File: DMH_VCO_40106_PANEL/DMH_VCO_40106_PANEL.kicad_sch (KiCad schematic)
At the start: 35 parts, among them J1 GND

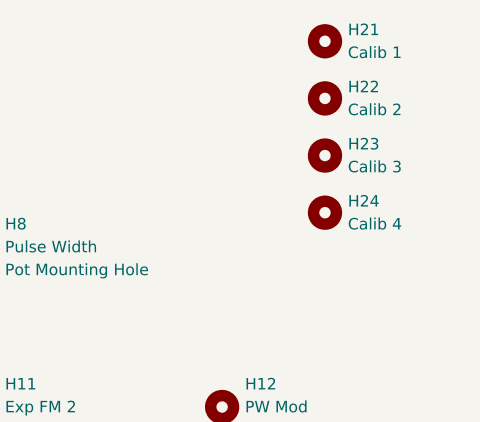
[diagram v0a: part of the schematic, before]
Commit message: Updated pot mounting hole sizes
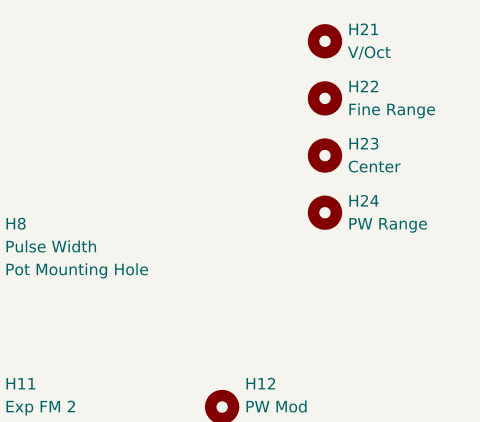
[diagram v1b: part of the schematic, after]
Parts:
- H21: value Calib 1 -> V/Oct; footprint MountingHole:MountingHole_2.2mm_M2_DIN965 -> MountingHole:MountingHole_2.5mm
- H22: value Calib 2 -> Fine Range; footprint MountingHole:MountingHole_2.2mm_M2_DIN965 -> MountingHole:MountingHole_2.5mm
- H23: value Calib 3 -> Center; footprint MountingHole:MountingHole_2.2mm_M2_DIN965 -> MountingHole:MountingHole_2.5mm
- H24: value Calib 4 -> PW Range; footprint MountingHole:MountingHole_2.2mm_M2_DIN965 -> MountingHole:MountingHole_2.5mm
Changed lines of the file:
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@@
 			)
 		)
-		(property "Value" "Calib 3"
+		(property "Value" "Center"
 			(at 180.34 31.7499 0)
 			(effects
@@
 			)
 		)
-		(property "Footprint" "MountingHole:MountingHole_2.2mm_M2_DIN965"
+		(property "Footprint" "MountingHole:MountingHole_2.5mm"
 			(at 177.8 30.48 0)
 			(effects
@@
 			)
 		)
-		(property "Value" "Calib 1"
+		(property "Value" "V/Oct"
 			(at 180.34 19.0499 0)
 			(effects
@@
 			)
 		)
-		(property "Footprint" "MountingHole:MountingHole_2.2mm_M2_DIN965"
+		(property "Footprint" "MountingHole:MountingHole_2.5mm"
 			(at 177.8 17.78 0)
 			(effects
@@
 			)
 		)
-		(property "Value" "Calib 4"
+		(property "Value" "PW Range"
 			(at 180.34 38.0999 0)
 			(effects
@@
 			)
 		)
-		(property "Footprint" "MountingHole:MountingHole_2.2mm_M2_DIN965"
+		(property "Footprint" "MountingHole:MountingHole_2.5mm"
 			(at 177.8 36.83 0)
 			(effects
@@
 			)
 		)
-		(property "Value" "Calib 2"
+		(property "Value" "Fine Range"
 			(at 180.34 25.3999 0)
 			(effects
@@
 			)
 		)
-		(property "Footprint" "MountingHole:MountingHole_2.2mm_M2_DIN965"
+		(property "Footprint" "MountingHole:MountingHole_2.5mm"
 			(at 177.8 24.13 0)
 			(effects

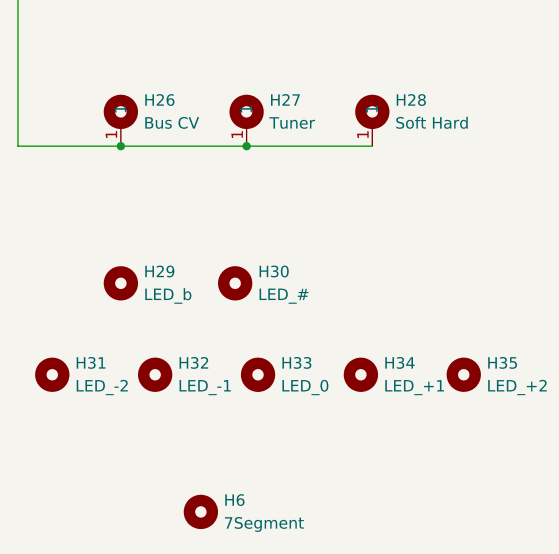
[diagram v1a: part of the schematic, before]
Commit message: Removed the flat sign LED
and rerouted segments A and B to PORTD 6 and 7 respective,
and rerouted the DP segment to PORTA0
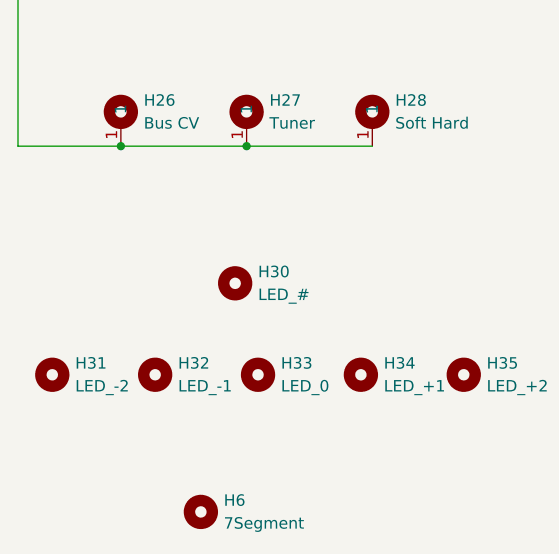
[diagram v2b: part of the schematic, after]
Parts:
- removed H29: LED_b, SynthStuff:MountingHole_LED_3mm, symbol Mechanical:MountingHole
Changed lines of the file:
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@@
-	)
-	(symbol
-		(lib_id "Mechanical:MountingHole")
-		(at 26.67 95.25 0)
-		(unit 1)
-		(exclude_from_sim yes)
-		(in_bom no)
-		(on_board yes)
-		(dnp no)
-		(fields_autoplaced yes)
-		(property "Reference" "H29"
-			(at 29.21 93.9799 0)
-			(effects
-				(font
-					(size 1.27 1.27)
-				)
-				(justify left)
-			)
-		)
-		(property "Value" "LED_b"
-			(at 29.21 96.5199 0)
-			(effects
-				(font
-					(size 1.27 1.27)
-				)
-				(justify left)
-			)
-		)
-		(property "Footprint" "SynthStuff:MountingHole_LED_3mm"
-			(at 26.67 95.25 0)
-			(effects
-				(font
-					(size 1.27 1.27)
-				)
-				(hide yes)
-			)
-		)
-		(property "Datasheet" "~"
-			(at 26.67 95.25 0)
-			(effects
-				(font
-					(size 1.27 1.27)
-				)
-				(hide yes)
-			)
-		)
-		(property "Description" "Mounting Hole without connection"
-			(at 26.67 95.25 0)
-			(effects
-				(font
-					(size 1.27 1.27)
-				)
-				(hide yes)
-			)
-		)
-		(instances
-			(project ""
-				(path "/1ac843a2-b018-4f05-9c7c-f861332ffc39"
-					(reference "H29")
-					(unit 1)
-				)
-			)
-		)
 	)
 	(symbol

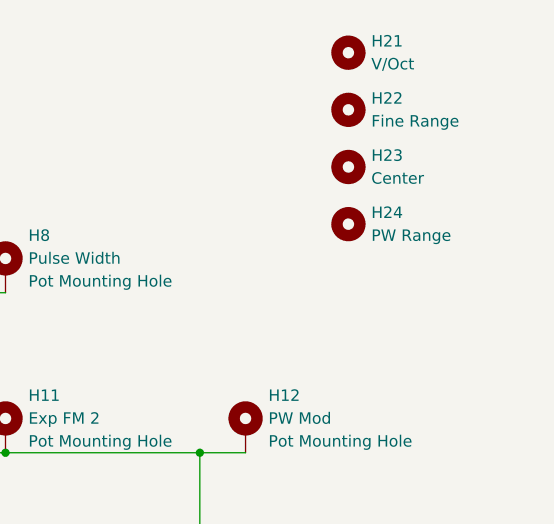
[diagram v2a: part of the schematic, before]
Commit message: Used Mounting Hole Trimpot symbol
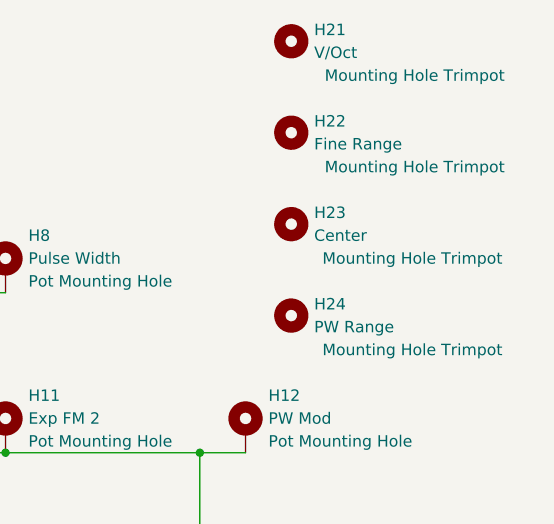
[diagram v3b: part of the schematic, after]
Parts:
- H21, H22, H23, H24: symbol Mechanical:MountingHole -> SynthStuff:MountingHole_Trimpot
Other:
- moved on the sheet: H21, H22, H23, H24
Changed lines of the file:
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@@
 	)
 	(symbol
-		(lib_id "Mechanical:MountingHole")
-		(at 177.8 30.48 0)
-		(unit 1)
-		(exclude_from_sim yes)
-		(in_bom no)
-		(on_board yes)
-		(dnp no)
-		(fields_autoplaced yes)
+		(lib_id "SynthStuff:MountingHole_Trimpot")
+		(at 171.45 36.83 0)
+		(unit 1)
+		(exclude_from_sim yes)
+		(in_bom no)
+		(on_board yes)
+		(dnp no)
 		(property "Reference" "H23"
-			(at 180.34 29.2099 0)
+			(at 173.99 35.5599 0)
 			(effects
 				(font
@@
 		)
 		(property "Value" "Center"
-			(at 180.34 31.7499 0)
+			(at 173.99 38.0999 0)
 			(effects
 				(font
@@
 		)
 		(property "Footprint" "MountingHole:MountingHole_2.5mm"
-			(at 177.8 30.48 0)
-			(effects
-				(font
-					(size 1.27 1.27)
-				)
-				(hide yes)
-			)
-		)
-		(property "Datasheet" "~"
-			(at 177.8 30.48 0)
-			(effects
-				(font
-					(size 1.27 1.27)
-				)
-				(hide yes)
-			)
-		)
-		(property "Description" "Mounting Hole without connection"
-			(at 177.8 30.48 0)
-			(effects
-				(font
-					(size 1.27 1.27)
-				)
-				(hide yes)
+			(at 171.45 36.83 0)
+			(effects
+				(font
+					(size 1.27 1.27)
+				)
+				(hide yes)
+			)
+		)
+		(property "Datasheet" "~"
+			(at 171.45 36.83 0)
+			(effects
+				(font
+					(size 1.27 1.27)
+				)
+				(hide yes)
+			)
+		)
+		(property "Description" "Mounting Hole Trimpot"
+			(at 184.912 40.64 0)
+			(effects
+				(font
+					(size 1.27 1.27)
+				)
 			)
 		)
@@
 	)
 	(symbol
-		(lib_id "Mechanical:MountingHole")
-		(at 177.8 17.78 0)
-		(unit 1)
-		(exclude_from_sim yes)
-		(in_bom no)
-		(on_board yes)
-		(dnp no)
-		(fields_autoplaced yes)
+		(lib_id "SynthStuff:MountingHole_Trimpot")
+		(at 171.45 16.51 0)
+		(unit 1)
+		(exclude_from_sim yes)
+		(in_bom no)
+		(on_board yes)
+		(dnp no)
 		(property "Reference" "H21"
-			(at 180.34 16.5099 0)
+			(at 173.99 15.2399 0)
 			(effects
 				(font
@@
 		)
 		(property "Value" "V/Oct"
-			(at 180.34 19.0499 0)
+			(at 173.99 17.7799 0)
 			(effects
 				(font
@@
 		)
 		(property "Footprint" "MountingHole:MountingHole_2.5mm"
-			(at 177.8 17.78 0)
-			(effects
-				(font
-					(size 1.27 1.27)
-				)
-				(hide yes)
-			)
-		)
-		(property "Datasheet" "~"
-			(at 177.8 17.78 0)
-			(effects
-				(font
-					(size 1.27 1.27)
-				)
-				(hide yes)
-			)
-		)
-		(property "Description" "Mounting Hole without connection"
-			(at 177.8 17.78 0)
-			(effects
-				(font
-					(size 1.27 1.27)
-				)
-				(hide yes)
+			(at 171.45 16.51 0)
+			(effects
+				(font
+					(size 1.27 1.27)
+				)
+				(hide yes)
+			)
+		)
+		(property "Datasheet" "~"
+			(at 171.45 16.51 0)
+			(effects
+				(font
+					(size 1.27 1.27)
+				)
+				(hide yes)
+			)
+		)
+		(property "Description" "Mounting Hole Trimpot"
+			(at 185.166 20.32 0)
+			(effects
+				(font
+					(size 1.27 1.27)
+				)
 			)
 		)
@@
 	)
 	(symbol
-		(lib_id "Mechanical:MountingHole")
-		(at 177.8 36.83 0)
-		(unit 1)
-		(exclude_from_sim yes)
-		(in_bom no)
-		(on_board yes)
-		(dnp no)
-		(fields_autoplaced yes)
+		(lib_id "SynthStuff:MountingHole_Trimpot")
+		(at 171.45 46.99 0)
+		(unit 1)
+		(exclude_from_sim yes)
+		(in_bom no)
+		(on_board yes)
+		(dnp no)
 		(property "Reference" "H24"
-			(at 180.34 35.5599 0)
+			(at 173.99 45.7199 0)
 			(effects
 				(font
@@
 		)
 		(property "Value" "PW Range"
-			(at 180.34 38.0999 0)
+			(at 173.99 48.2599 0)
 			(effects
 				(font
@@
 		)
 		(property "Footprint" "MountingHole:MountingHole_2.5mm"
-			(at 177.8 36.83 0)
-			(effects
-				(font
-					(size 1.27 1.27)
-				)
-				(hide yes)
-			)
-		)
-		(property "Datasheet" "~"
-			(at 177.8 36.83 0)
-			(effects
-				(font
-					(size 1.27 1.27)
-				)
-				(hide yes)
-			)
-		)
-		(property "Description" "Mounting Hole without connection"
-			(at 177.8 36.83 0)
-			(effects
-				(font
-					(size 1.27 1.27)
-				)
-				(hide yes)
+			(at 171.45 46.99 0)
+			(effects
+				(font
+					(size 1.27 1.27)
+				)
+				(hide yes)
+			)
+		)
+		(property "Datasheet" "~"
+			(at 171.45 46.99 0)
+			(effects
+				(font
+					(size 1.27 1.27)
+				)
+				(hide yes)
+			)
+		)
+		(property "Description" "Mounting Hole Trimpot"
+			(at 184.912 50.8 0)
+			(effects
+				(font
+					(size 1.27 1.27)
+				)
 			)
 		)
@@
 	)
 	(symbol
-		(lib_id "Mechanical:MountingHole")
-		(at 177.8 24.13 0)
-		(unit 1)
-		(exclude_from_sim yes)
-		(in_bom no)
-		(on_board yes)
-		(dnp no)
-		(fields_autoplaced yes)
+		(lib_id "SynthStuff:MountingHole_Trimpot")
+		(at 171.45 26.67 0)
+		(unit 1)
+		(exclude_from_sim yes)
+		(in_bom no)
+		(on_board yes)
+		(dnp no)
 		(property "Reference" "H22"
-			(at 180.34 22.8599 0)
+			(at 173.99 25.3999 0)
 			(effects
 				(font
@@
 		)
 		(property "Value" "Fine Range"
-			(at 180.34 25.3999 0)
+			(at 173.99 27.9399 0)
 			(effects
 				(font
@@
 		)
 		(property "Footprint" "MountingHole:MountingHole_2.5mm"
-			(at 177.8 24.13 0)
-			(effects
-				(font
-					(size 1.27 1.27)
-				)
-				(hide yes)
-			)
-		)
-		(property "Datasheet" "~"
-			(at 177.8 24.13 0)
-			(effects
-				(font
-					(size 1.27 1.27)
-				)
-				(hide yes)
-			)
-		)
-		(property "Description" "Mounting Hole without connection"
-			(at 177.8 24.13 0)
-			(effects
-				(font
-					(size 1.27 1.27)
-				)
-				(hide yes)
-			)
-		)
+			(at 171.45 26.67 0)
+			(effects
+				(font
+					(size 1.27 1.27)
+				)
+				(hide yes)
+			)
+		)
+		(property "Datasheet" "~"
+			(at 171.45 26.67 0)
+			(effects
+				(font
+					(size 1.27 1.27)
+				)
+				(hide yes)
+			)
+		)
+		(property "Description" "Mounting Hole Trimpot"
+			(at 185.166 30.48 0)
+			(effects
+				(font
+					(size 1.27 1.27)
+				)
+			)
+		)

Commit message: Synced with trimpot mounting hole footprint
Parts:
- H21, H22, H23, H24: footprint MountingHole:MountingHole_2.5mm -> SynthStuff:MountingHole_TrimPot
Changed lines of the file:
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@@
 			)
 		)
-		(property "Footprint" "MountingHole:MountingHole_2.5mm"
+		(property "Footprint" "SynthStuff:MountingHole_TrimPot"
 			(at 171.45 36.83 0)
 			(effects
@@
 			)
 		)
-		(property "Footprint" "MountingHole:MountingHole_2.5mm"
+		(property "Footprint" "SynthStuff:MountingHole_TrimPot"
 			(at 171.45 16.51 0)
 			(effects
@@
 			)
 		)
-		(property "Footprint" "MountingHole:MountingHole_2.5mm"
+		(property "Footprint" "SynthStuff:MountingHole_TrimPot"
 			(at 171.45 46.99 0)
 			(effects
@@
 			)
 		)
-		(property "Footprint" "MountingHole:MountingHole_2.5mm"
+		(property "Footprint" "SynthStuff:MountingHole_TrimPot"
 			(at 171.45 26.67 0)
 			(effects
